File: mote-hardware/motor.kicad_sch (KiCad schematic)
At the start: 10 parts, among them J7 JST_PH_B6B, J8 JST_PH_B6B, U5 DRV8833PW

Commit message: Add position corrections
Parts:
- C19, C2, C20, C21, J7, J8, R11, R12: JLCPCB_CORRECTION (none) -> 0; 0; 0
- C22: value 0.1u -> 100n; JLCPCB_CORRECTION (none) -> 0; 0; 0
- U5: JLCPCB_CORRECTION (none) -> 0; 0; 270
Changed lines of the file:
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@@
 			)
 		)
-		(property "JLCPCB_CORRECTION" ""
+		(property "JLCPCB_CORRECTION" "0; 0; 0"
 			(at 166.37 67.31 0)
 			(effects
@@
 			)
 		)
-		(property "JLCPCB_CORRECTION" ""
+		(property "JLCPCB_CORRECTION" "0; 0; 0"
 			(at 180.34 67.31 0)
 			(effects
@@
 			)
 		)
-		(property "Value" "0.1u"
+		(property "Value" "100n"
 			(at 194.056 70.104 0)
 			(effects
@@
 			)
 		)
-		(property "JLCPCB_CORRECTION" ""
+		(property "JLCPCB_CORRECTION" "0; 0; 0"
 			(at 193.04 67.31 0)
 			(effects
@@
 			)
 		)
-		(property "JLCPCB_CORRECTION" ""
+		(property "JLCPCB_CORRECTION" "0; 0; 0"
 			(at 198.12 125.73 0)
 			(effects
@@
 			)
 		)
-		(property "JLCPCB_CORRECTION" ""
+		(property "JLCPCB_CORRECTION" "0; 0; 0"
 			(at 198.12 104.14 0)
 			(effects
@@
 			)
 		)
-		(property "JLCPCB_CORRECTION" ""
+		(property "JLCPCB_CORRECTION" "0; 0; 0"
 			(at 127 104.14 90)
 			(effects
@@
 			)
 		)
-		(property "JLCPCB_CORRECTION" ""
+		(property "JLCPCB_CORRECTION" "0; 0; 270"
 			(at 152.4 106.68 0)
 			(effects
@@
 			)
 		)
-		(property "JLCPCB_CORRECTION" ""
+		(property "JLCPCB_CORRECTION" "0; 0; 0"
 			(at 138.43 81.28 0)
 			(effects
@@
 			)
 		)
-		(property "JLCPCB_CORRECTION" ""
+		(property "JLCPCB_CORRECTION" "0; 0; 0"
 			(at 127 101.6 90)
 			(effects
@@
 			)
 		)
-		(property "JLCPCB_CORRECTION" ""
+		(property "JLCPCB_CORRECTION" "0; 0; 0"
 			(at 168.91 88.9 0)
 			(effects

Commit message: Update offsets
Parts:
- J7, J8: JLCPCB_CORRECTION 0; 0; 0 -> 4.953; 0; 0
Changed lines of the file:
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@@
 			)
 		)
-		(property "JLCPCB_CORRECTION" "0; 0; 0"
+		(property "JLCPCB_CORRECTION" "4.953; 0; 0"
 			(at 198.12 125.73 0)
 			(effects
@@
 			)
 		)
-		(property "JLCPCB_CORRECTION" "0; 0; 0"
+		(property "JLCPCB_CORRECTION" "4.953; 0; 0"
 			(at 198.12 104.14 0)
 			(effects

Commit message: Add GHA workflows for generating PDFs
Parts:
- J7, J8: JLCPCB_CORRECTION 4.953; 0; 0 -> 4.8895; 0; 0
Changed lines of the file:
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@@
 			)
 		)
-		(property "JLCPCB_CORRECTION" "4.953; 0; 0"
+		(property "JLCPCB_CORRECTION" "4.8895; 0; 0"
 			(at 198.12 125.73 0)
 			(effects
@@
 			)
 		)
-		(property "JLCPCB_CORRECTION" "4.953; 0; 0"
+		(property "JLCPCB_CORRECTION" "4.8895; 0; 0"
 			(at 198.12 104.14 0)
 			(effects

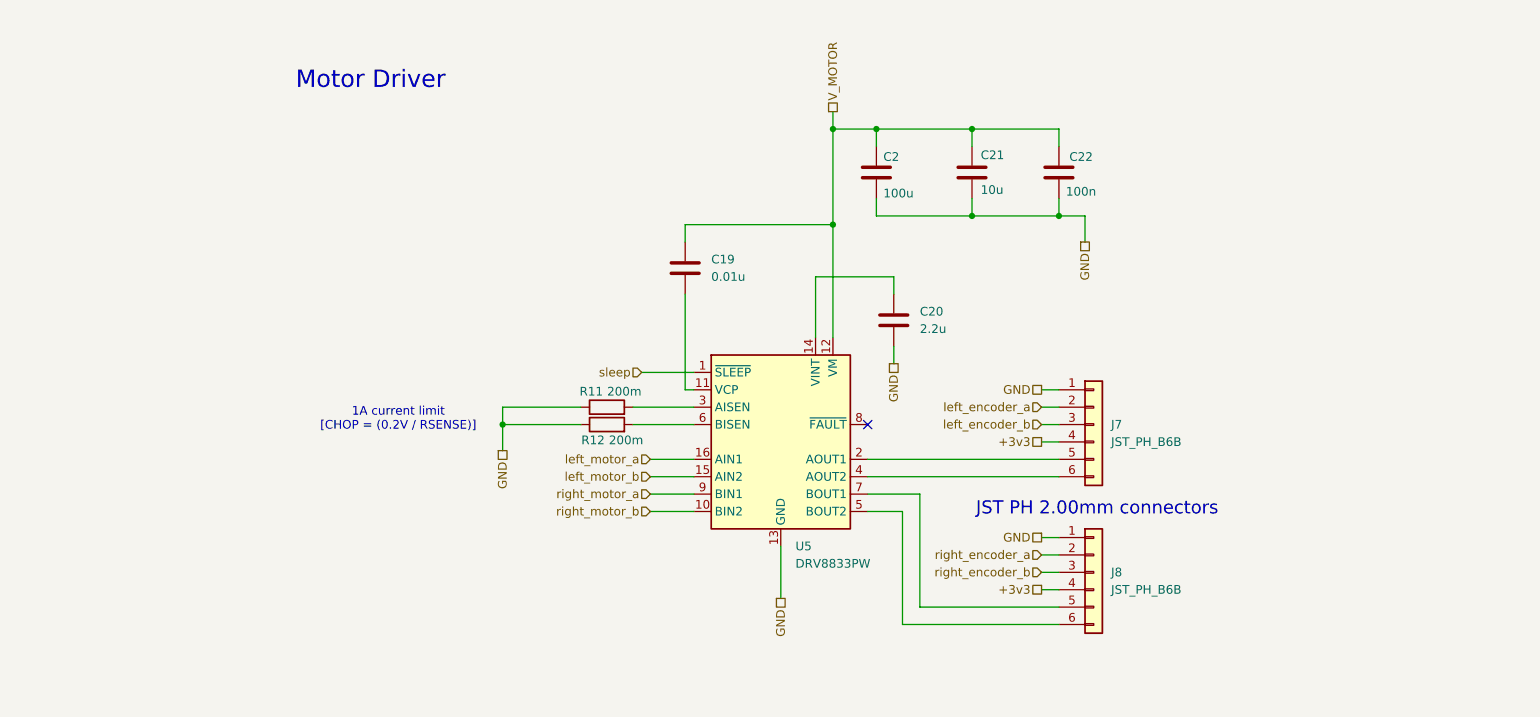
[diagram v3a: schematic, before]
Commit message: Add TVS diodes
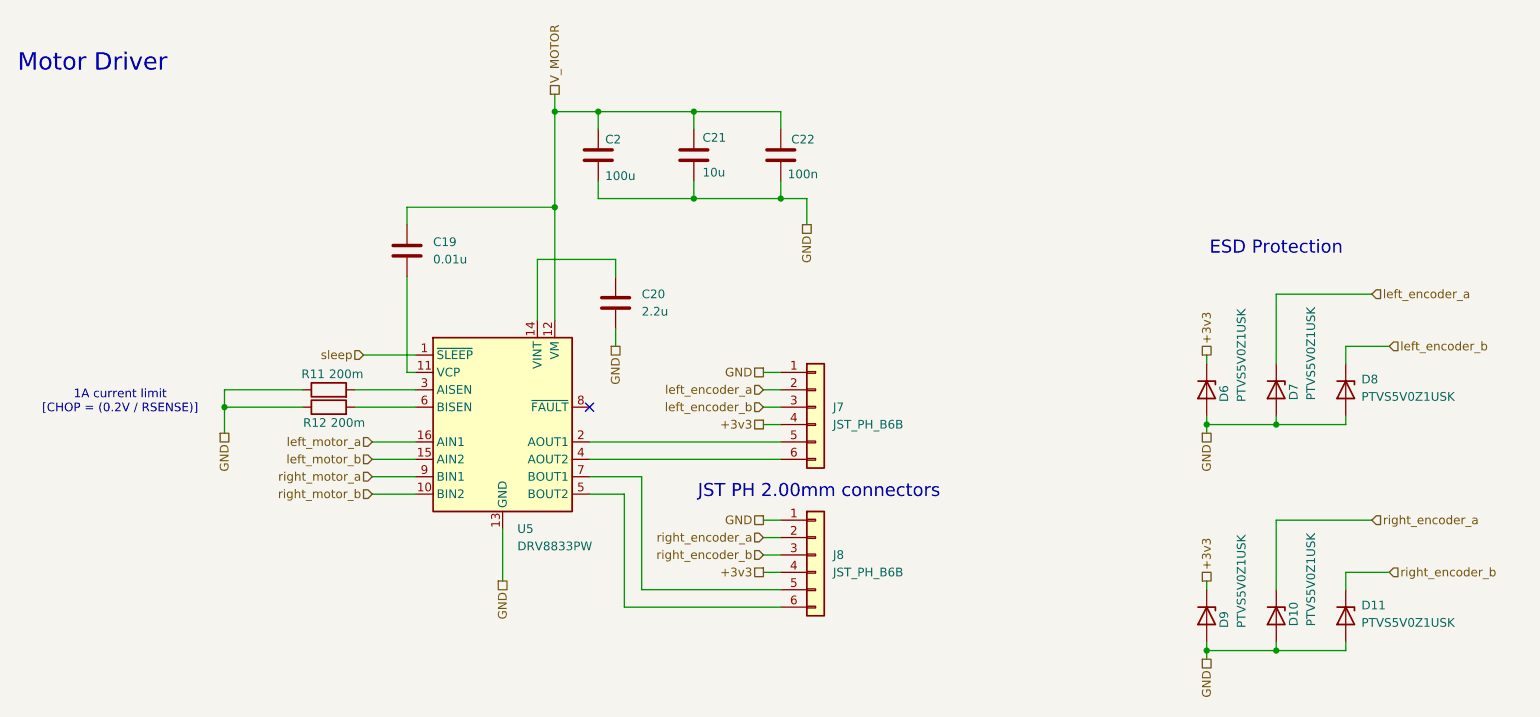
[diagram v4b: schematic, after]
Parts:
- added D10, D11, D6, D7, D8, D9: PTVS5V0Z1USK, Diode_SMD:Nexperia_DSN1608-2_1.6x0.8mm, symbol Diode:PTVS5V0Z1USK
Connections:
- net +3v3: now also D6.1 (K), D9.1 (K)
- net GND: now also D10.2 (A), D11.2 (A), D6.2 (A), D7.2 (A), D8.2 (A), D9.2 (A)
- net left_encoder_a: now also D7.1 (K)
- net left_encoder_b: now also D8.1 (K)
- net right_encoder_a: now also D10.1 (K)
- net right_encoder_b: now also D11.1 (K)
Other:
- note added: "ESD Protection"
- moved on the sheet: C19, C2, C20, C21, C22, J7, J8, R11, R12, U5

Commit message: Layout for TVs diodes
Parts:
- D10, D11, D6, D7, D8, D9: value PTVS5V0Z1USK -> PTVS5V0S1UR-FS; footprint Diode_SMD:Nexperia_DSN1608-2_1.6x0.8mm -> Diode_SMD:D_SOD-123; JLCPCB_CORRECTION (none) -> 0; 0; 0; LCSC (none) -> C5380694
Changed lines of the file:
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@@
 			)
 		)
-		(property "Value" "PTVS5V0Z1USK"
+		(property "Value" "PTVS5V0S1UR-FS"
 			(at 219.71 100.838 0)
 			(effects
@@
 			)
 		)
-		(property "Footprint" "Diode_SMD:Nexperia_DSN1608-2_1.6x0.8mm"
+		(property "Footprint" "Diode_SMD:D_SOD-123"
 			(at 210.185 99.06 0)
 			(effects
@@
 			)
 		)
+		(property "JLCPCB_CORRECTION" "0; 0; 0"
+			(at 214.63 99.06 0)
+			(effects
+				(font
+					(size 1.27 1.27)
+				)
+				(hide yes)
+			)
+		)
+		(property "LCSC" "C5380694"
+			(at 214.63 99.06 0)
+			(effects
+				(font
+					(size 1.27 1.27)
+				)
+				(hide yes)
+			)
+		)
 		(pin "1"
 		)
@@
 			)
 		)
-		(property "Value" "PTVS5V0Z1USK"
+		(property "Value" "PTVS5V0S1UR-FS"
 			(at 237.236 100.076 90)
 			(effects
@@
 			)
 		)
-		(property "Footprint" "Diode_SMD:Nexperia_DSN1608-2_1.6x0.8mm"
+		(property "Footprint" "Diode_SMD:D_SOD-123"
 			(at 230.505 99.06 0)
 			(effects
@@
 		(property "Description" "5V, 1200W TVS unidirectional diode, DSN1608-2"
 			(at 234.95 99.06 0)
+			(effects
+				(font
+					(size 1.27 1.27)
+				)
+				(hide yes)
+			)
+		)
+		(property "JLCPCB_CORRECTION" "0; 0; 0"
+			(at 234.95 99.06 90)
+			(effects
+				(font
+					(size 1.27 1.27)
+				)
+				(hide yes)
+			)
+		)
+		(property "LCSC" "C5380694"
+			(at 234.95 99.06 90)
 			(effects
 				(font
@@
 			)
 		)
-		(property "Value" "PTVS5V0Z1USK"
+		(property "Value" "PTVS5V0S1UR-FS"
 			(at 229.87 100.584 0)
 			(effects
@@
 			)
 		)
-		(property "Footprint" "Diode_SMD:Nexperia_DSN1608-2_1.6x0.8mm"
+		(property "Footprint" "Diode_SMD:D_SOD-123"
 			(at 220.345 99.06 0)
 			(effects
@@
 			)
 		)
+		(property "JLCPCB_CORRECTION" "0; 0; 0"
+			(at 224.79 99.06 0)
+			(effects
+				(font
+					(size 1.27 1.27)
+				)
+				(hide yes)
+			)
+		)
+		(property "LCSC" "C5380694"
+			(at 224.79 99.06 0)
+			(effects
+				(font
+					(size 1.27 1.27)
+				)
+				(hide yes)
+			)
+		)
 		(pin "1"
 		)
@@
 			)
 		)
-		(property "Value" "PTVS5V0Z1USK"
+		(property "Value" "PTVS5V0S1UR-FS"
 			(at 219.71 133.858 0)
 			(effects
@@
 			)
 		)
-		(property "Footprint" "Diode_SMD:Nexperia_DSN1608-2_1.6x0.8mm"
+		(property "Footprint" "Diode_SMD:D_SOD-123"
 			(at 210.185 132.08 0)
 			(effects
@@
 			)
 		)
+		(property "JLCPCB_CORRECTION" "0; 0; 0"
+			(at 214.63 132.08 0)
+			(effects
+				(font
+					(size 1.27 1.27)
+				)
+				(hide yes)
+			)
+		)
+		(property "LCSC" "C5380694"
+			(at 214.63 132.08 0)
+			(effects
+				(font
+					(size 1.27 1.27)
+				)
+				(hide yes)
+			)
+		)
 		(pin "1"
 		)
@@
 			)
 		)
-		(property "Value" "PTVS5V0Z1USK"
+		(property "Value" "PTVS5V0S1UR-FS"
 			(at 229.87 133.604 0)
 			(effects
@@
 			)
 		)
-		(property "Footprint" "Diode_SMD:Nexperia_DSN1608-2_1.6x0.8mm"
+		(property "Footprint" "Diode_SMD:D_SOD-123"
 			(at 220.345 132.08 0)
 			(effects
@@
 			)
 		)
+		(property "JLCPCB_CORRECTION" "0; 0; 0"
+			(at 224.79 132.08 0)
+			(effects
+				(font
+					(size 1.27 1.27)
+				)
+				(hide yes)
+			)
+		)
+		(property "LCSC" "C5380694"
+			(at 224.79 132.08 0)
+			(effects
+				(font
+					(size 1.27 1.27)
+				)
+				(hide yes)
+			)
+		)
 		(pin "1"
 		)
@@
 			)
 		)
-		(property "Value" "PTVS5V0Z1USK"
+		(property "Value" "PTVS5V0S1UR-FS"
 			(at 237.236 133.096 90)
 			(effects
@@
 			)
 		)
-		(property "Footprint" "Diode_SMD:Nexperia_DSN1608-2_1.6x0.8mm"
+		(property "Footprint" "Diode_SMD:D_SOD-123"
 			(at 230.505 132.08 0)
 			(effects
@@
 			(effects
 				(font
+					(size 1.27 1.27)
+				)
+				(hide yes)
+			)
+		)
+		(property "JLCPCB_CORRECTION" "0; 0; 0"
+			(at 234.95 132.08 90)
+			(effects
+				(font
+					(size 1.27 1.27)
+				)
+				(hide yes)
+			)
+		)
+		(property "LCSC" "C5380694"
+			(at 234.95 132.08 90)
+			(effects
+				(font
